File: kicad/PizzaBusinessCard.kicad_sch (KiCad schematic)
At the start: 16 parts, among them SW1 ON / OFF, U1 4017

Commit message: implement with NE555
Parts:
- removed D1: LED, LED_SMD:LED_0805_2012Metric_Pad1.15x1.40mm_HandSolder, symbol Device:LED
- added C1: 10nF, Capacitor_SMD:C_0805_2012Metric_Pad1.18x1.45mm_HandSolder, symbol Device:C
- added C2: 10uF, Capacitor_SMD:C_0805_2012Metric_Pad1.18x1.45mm_HandSolder, symbol Device:C
- added R3: 10K, Resistor_SMD:R_0805_2012Metric_Pad1.20x1.40mm_HandSolder, symbol Device:R
- added U2: NE555D, Package_SO:SOIC-8_3.9x4.9mm_P1.27mm, symbol Timer:NE555D
- R1: value 470 -> 10K
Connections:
- net LED11 is gone; now on net LED10: D11.2 (A), U1.11 (Q9)
- net GND: now also C1.2, C2.2, U2.1 (GND); no longer R1.1
- net LED1: now also U1.3 (Q0); no longer U1.1 (Q5)
- net LED10: no longer D10.2 (A), U1.10 (Q4)
- net LED3: now also U1.4 (Q2); no longer U1.3 (Q0)
- net LED4: now also U1.7 (Q3); no longer U1.4 (Q2)
- net LED5: now also U1.10 (Q4); no longer U1.5 (Q6)
- net LED6: now also U1.1 (Q5); no longer U1.6 (Q7)
- net LED7: now also U1.5 (Q6); no longer U1.7 (Q3)
- net LED9: now also D10.2 (A); no longer D9.2 (A)
- net BUTTON renamed 5V
- net 5V: now also R1.2, U2.4 (R), U2.8 (VCC)
- net LED_RGB renamed CLOCK
- net CLOCK: now also U2.3 (Q); no longer R1.2
- new net: C2.1, R3.1, U2.2 (TR), U2.6 (THR)
- new net: C1.1, U2.5 (CV)
- new net: R1.1, R3.2, U2.7 (DIS)
- new net LED8: D9.2 (A), U1.6 (Q7)

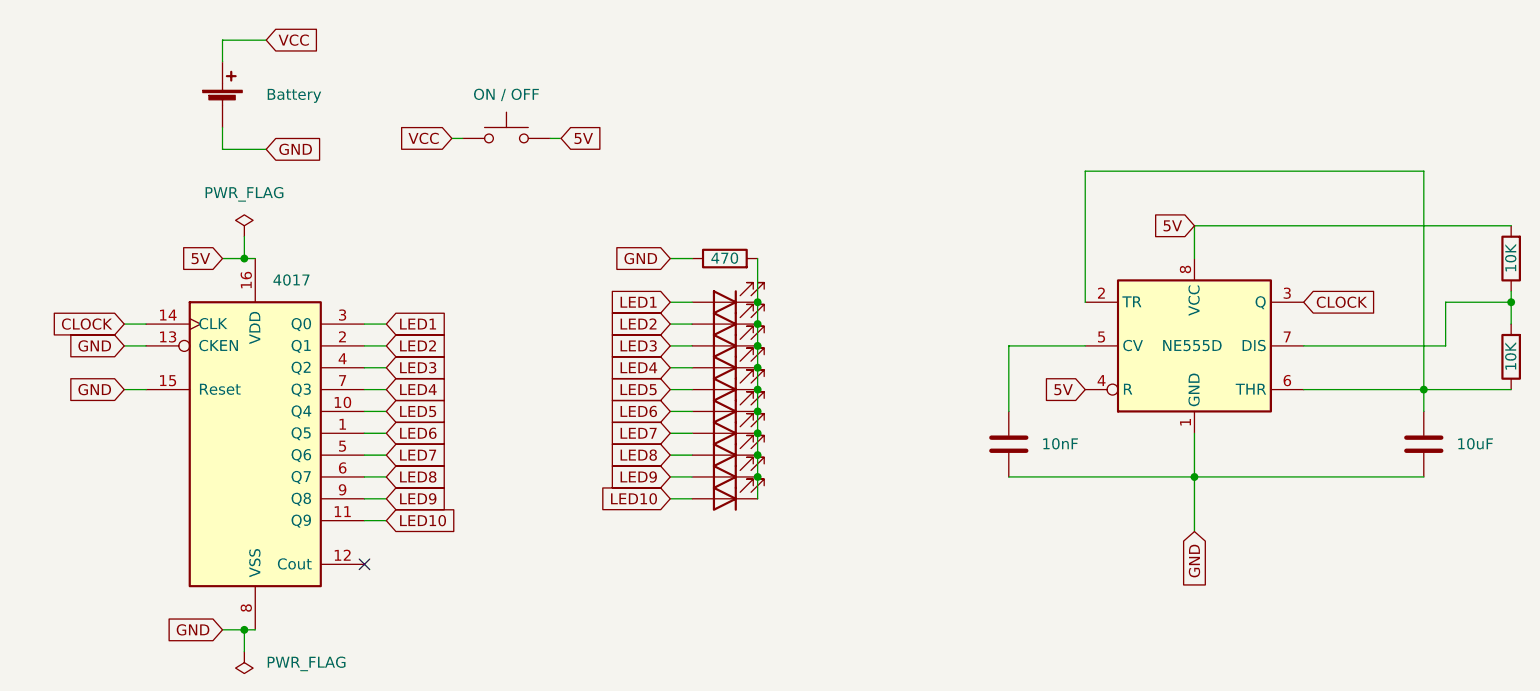
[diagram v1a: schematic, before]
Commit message: simplify ne555
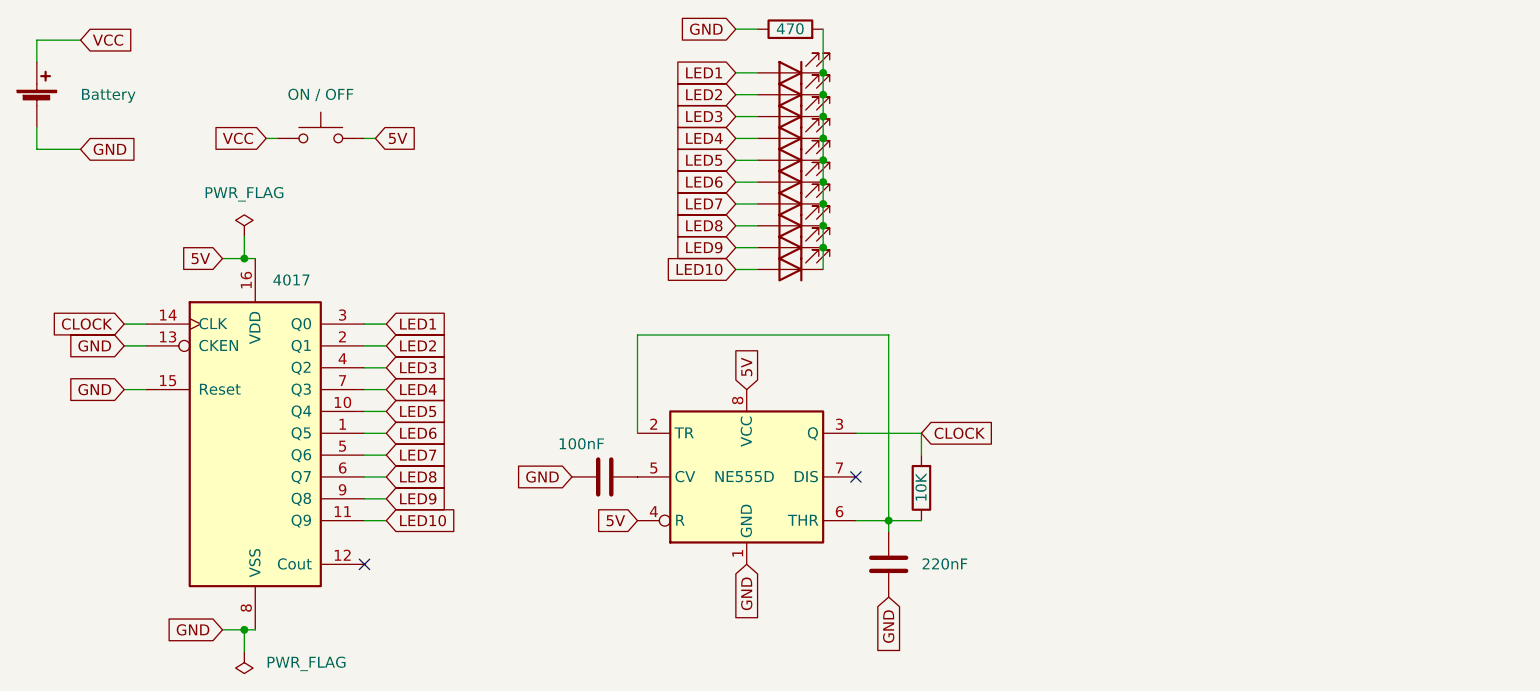
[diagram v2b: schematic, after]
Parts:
- removed R1: 10K, Resistor_SMD:R_0805_2012Metric_Pad1.20x1.40mm_HandSolder, symbol Device:R
- C1: value 10nF -> 100nF
- C2: value 10uF -> 220nF
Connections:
- net CLOCK: now also R3.2
- net GND: now also C1.1; no longer C1.2
- net at U2.5 (CV): now also C1.2; no longer C1.1
- net at U2.7 (DIS): no longer R3.2
- no-connect marks 1 -> 2

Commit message: fix ne555
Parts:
- removed C1: 100nF, Capacitor_SMD:C_0805_2012Metric_Pad1.18x1.45mm_HandSolder, symbol Device:C
- added R1: 10K, Resistor_SMD:R_0805_2012Metric_Pad1.20x1.40mm_HandSolder, symbol Device:R
- C2: value 220nF -> 10uF
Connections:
- net 5V: now also R1.1
- net CLOCK: no longer R3.2
- net at U2.7 (DIS): now also R3.2, R1.2
